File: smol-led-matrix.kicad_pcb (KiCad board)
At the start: 4 copper layers, 46.4 x 20.4 mm, 320 parts, among them J1 USB_C_Receptacle_USB2.0, J2 TagConnect_TC2030_SWD, Q1 FS8205, Q2 AO3401A, SW1 SW_Push, SW2 SW_Push, U1 STM32L433CBTx, U2 TP4054, U3 DW01+G, U4 XC6206P332MR

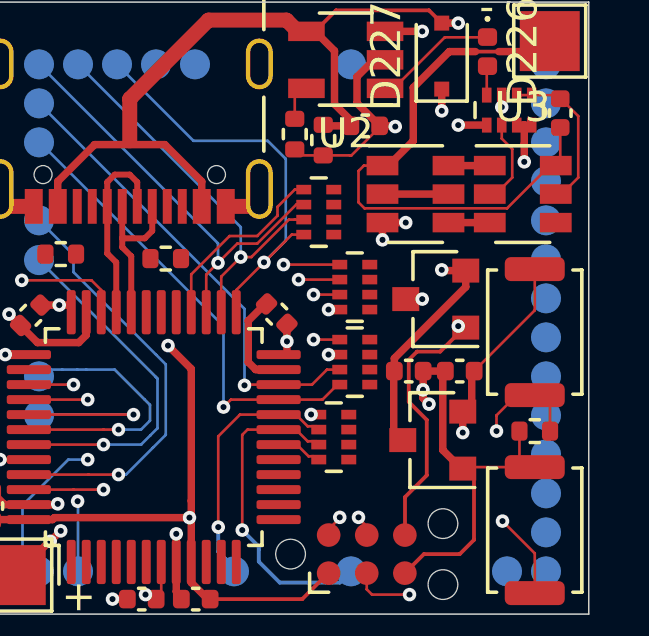
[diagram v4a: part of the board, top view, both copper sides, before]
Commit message: Layout straight forward anode controls
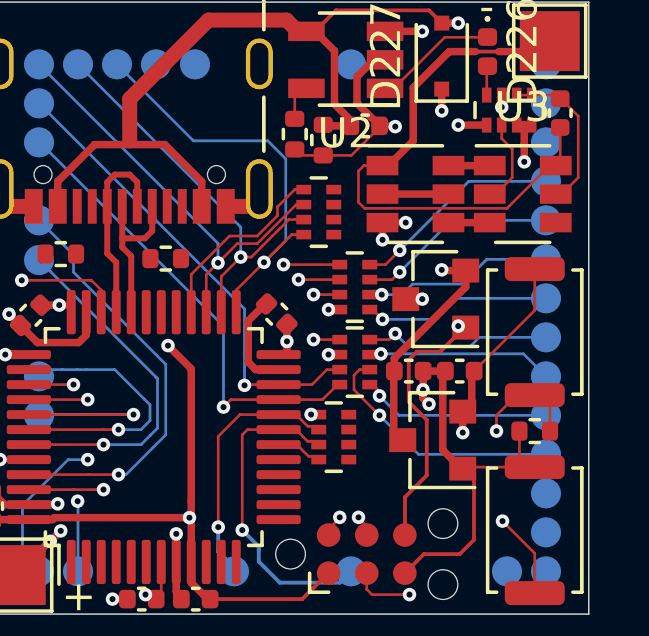
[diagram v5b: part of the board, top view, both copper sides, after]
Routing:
- net /A11: track 19.9 -> 28.3 mm, vias 1 -> 2
- net /A4: track 19.9 -> 26.9 mm, vias 1 -> 2
- net /A5: track 19.9 -> 26.6 mm, vias 1 -> 2
- net /A8: track 19.9 -> 26.6 mm, vias 1 -> 2
- net /A10: track 19.9 -> 26.3 mm, vias 1 -> 2
- net /A6: track 19.9 -> 26.3 mm, vias 1 -> 2
- net /A7: track 19.9 -> 26.2 mm, vias 1 -> 2
- net /A9: track 19.9 -> 26.1 mm, vias 1 -> 2
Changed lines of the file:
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@@
     (thickness 1.6)
     (drawings 11)
-    (tracks 1141)
+    (tracks 1190)
     (zones 0)
     (modules 320)
@@
   (via (at 102.3 103.55) (size 0.45) (drill 0.2) (layers F.Cu B.Cu) (net 6))
   (segment (start 101 103.549999) (end 102.3 103.55) (width 0.09) (layer B.Cu) (net 6))
+  (via (at 139.675 105.85) (size 0.45) (drill 0.2) (layers F.Cu B.Cu) (net 6))
+  (segment (start 139.2 106.325) (end 139.675 105.85) (width 0.09) (layer F.Cu) (net 6))
+  (segment (start 138.675 106.325) (end 139.2 106.325) (width 0.09) (layer F.Cu) (net 6))
+  (segment (start 141.975 103.55) (end 139.675 105.85) (width 0.09) (layer B.Cu) (net 6))
+  (segment (start 144.55 103.55) (end 141.975 103.55) (width 0.09) (layer B.Cu) (net 6))
   (segment (start 106.217947 104.832052) (end 106.867947 104.832053) (width 0.09) (layer F.Cu) (net 7))
   (segment (start 108.132053 104.832053) (end 108.817947 104.832053) (width 0.09) (layer F.Cu) (net 7))
@@
   (via (at 102.3 104.85) (size 0.45) (drill 0.2) (layers F.Cu B.Cu) (net 7))
   (segment (start 101 104.85) (end 102.3 104.85) (width 0.09) (layer B.Cu) (net 7))
+  (via (at 139.675 106.575) (size 0.45) (drill 0.2) (layers F.Cu B.Cu) (net 7))
+  (segment (start 139.425 106.825) (end 139.675 106.575) (width 0.09) (layer F.Cu) (net 7))
+  (segment (start 138.675 106.825) (end 139.425 106.825) (width 0.09) (layer F.Cu) (net 7))
+  (segment (start 141.4 104.85) (end 139.675 106.575) (width 0.09) (layer B.Cu) (net 7))
+  (segment (start 144.55 104.85) (end 141.4 104.85) (width 0.09) (layer B.Cu) (net 7))
   (segment (start 107.517947 106.132053) (end 108.167947 106.132054) (width 0.09) (layer F.Cu) (net 8))
   (segment (start 109.432053 106.132053) (end 110.117946 106.132054) (width 0.09) (layer F.Cu) (net 8))
@@
   (via (at 102.3 106.150001) (size 0.45) (drill 0.2) (layers F.Cu B.Cu) (net 8))
   (segment (start 101 106.15) (end 102.3 106.150001) (width 0.09) (layer B.Cu) (net 8))
+  (via (at 139.075 107.325) (size 0.45) (drill 0.2) (layers F.Cu B.Cu) (net 8))
+  (segment (start 138.675 107.325) (end 139.075 107.325) (width 0.09) (layer F.Cu) (net 8))
+  (segment (start 139.075 107.325) (end 139.75 107.325) (width 0.09) (layer B.Cu) (net 8))
+  (segment (start 139.75 107.325) (end 140.1 106.975) (width 0.09) (layer B.Cu) (net 8))
+  (segment (start 142.575 106.15) (end 141.75 106.975) (width 0.09) (layer B.Cu) (net 8))
+  (segment (start 144.55 106.15) (end 142.575 106.15) (width 0.09) (layer B.Cu) (net 8))
+  (segment (start 140.1 106.975) (end 141.75 106.975) (width 0.09) (layer B.Cu) (net 8))
   (segment (start 108.817948 107.432053) (end 109.467947 107.432053) (width 0.09) (layer F.Cu) (net 9))
   (segment (start 110.732053 107.432053) (end 111.417945 107.432053) (width 0.09) (layer F.Cu) (net 9))
@@
   (via (at 102.3 107.449999) (size 0.45) (drill 0.2) (layers F.Cu B.Cu) (net 9))
   (segment (start 101 107.45) (end 102.3 107.449999) (width 0.09) (layer B.Cu) (net 9))
+  (via (at 139.1 108.15) (size 0.45) (drill 0.2) (layers F.Cu B.Cu) (net 9))
+  (segment (start 138.775 107.825) (end 139.1 108.15) (width 0.09) (layer F.Cu) (net 9))
+  (segment (start 138.675 107.825) (end 138.775 107.825) (width 0.09) (layer F.Cu) (net 9))
+  (segment (start 144.55 107.45) (end 141.425 107.45) (width 0.09) (layer B.Cu) (net 9))
+  (segment (start 140.725 108.15) (end 139.1 108.15) (width 0.09) (layer B.Cu) (net 9))
+  (segment (start 141.425 107.45) (end 140.725 108.15) (width 0.09) (layer B.Cu) (net 9))
   (segment (start 110.117947 108.732053) (end 110.767947 108.732053) (width 0.09) (layer F.Cu) (net 10))
   (segment (start 112.032053 108.732053) (end 112.717947 108.732053) (width 0.09) (layer F.Cu) (net 10))
@@
   (via (at 102.3 108.75) (size 0.45) (drill 0.2) (layers F.Cu B.Cu) (net 10))
   (segment (start 101 108.75) (end 102.3 108.75) (width 0.09) (layer B.Cu) (net 10))
+  (via (at 139.525 108.625) (size 0.45) (drill 0.2) (layers F.Cu B.Cu) (net 10))
+  (segment (start 139.325 108.825) (end 139.525 108.625) (width 0.09) (layer F.Cu) (net 10))
+  (segment (start 138.675 108.825) (end 139.325 108.825) (width 0.09) (layer F.Cu) (net 10))
+  (segment (start 139.525 108.625) (end 139.95 109.05) (width 0.09) (layer B.Cu) (net 10))
+  (segment (start 144.25 109.05) (end 144.55 108.75) (width 0.09) (layer B.Cu) (net 10))
+  (segment (start 144.55 108.75) (end 142.325 108.75) (width 0.09) (layer B.Cu) (net 10))
+  (segment (start 142.325 108.75) (end 142.025 109.05) (width 0.09) (layer B.Cu) (net 10))
+  (segment (start 139.95 109.05) (end 142.025 109.05) (width 0.09) (layer B.Cu) (net 10))
   (segment (start 111.417947 110.032053) (end 112.067947 110.032053) (width 0.09) (layer F.Cu) (net 11))
   (segment (start 113.332053 110.032053) (end 114.017947 110.032054) (width 0.09) (layer F.Cu) (net 11))
@@
   (via (at 102.3 110.05) (size 0.45) (drill 0.2) (layers F.Cu B.Cu) (net 11))
   (segment (start 100.999999 110.050001) (end 102.3 110.05) (width 0.09) (layer B.Cu) (net 11))
+  (via (at 139.05 109.3) (size 0.45) (drill 0.2) (layers F.Cu B.Cu) (net 11))
+  (segment (start 139.025 109.325) (end 139.05 109.3) (width 0.09) (layer F.Cu) (net 11))
+  (segment (start 138.675 109.325) (end 139.025 109.325) (width 0.09) (layer F.Cu) (net 11))
+  (segment (start 139.05 109.3) (end 143.8 109.3) (width 0.09) (layer B.Cu) (net 11))
+  (segment (start 143.8 109.3) (end 144.55 110.05) (width 0.09) (layer B.Cu) (net 11))
   (segment (start 112.717947 111.332052) (end 113.367947 111.332053) (width 0.09) (layer F.Cu) (net 12))
   (segment (start 114.632053 111.332053) (end 115.317945 111.332053) (width 0.09) (layer F.Cu) (net 12))
@@
   (via (at 102.3 111.35) (size 0.45) (drill 0.2) (layers F.Cu B.Cu) (net 12))
   (segment (start 101 111.35) (end 102.3 111.35) (width 0.09) (layer B.Cu) (net 12))
+  (segment (start 138.675 110.325) (end 138.775 110.325) (width 0.09) (layer F.Cu) (net 12))
+  (via (at 139 110.7) (size 0.45) (drill 0.2) (layers F.Cu B.Cu) (net 12))
+  (segment (start 139 110.55) (end 139 110.7) (width 0.09) (layer F.Cu) (net 12))
+  (segment (start 138.775 110.325) (end 139 110.55) (width 0.09) (layer F.Cu) (net 12))
+  (segment (start 139.65 111.35) (end 139 110.7) (width 0.09) (layer B.Cu) (net 12))
+  (segment (start 144.55 111.35) (end 139.65 111.35) (width 0.09) (layer B.Cu) (net 12))
   (segment (start 114.017947 112.632053) (end 114.667947 112.632053) (width 0.09) (layer F.Cu) (net 13))
   (segment (start 115.932053 112.632053) (end 116.617947 112.632053) (width 0.09) (layer F.Cu) (net 13))
@@
   (via (at 102.3 112.65) (size 0.45) (drill 0.2) (layers F.Cu B.Cu) (net 13))
   (segment (start 101 112.65) (end 102.3 112.65) (width 0.09) (layer B.Cu) (net 13))
+  (segment (start 138.335 109.825) (end 138.15 110.01) (width 0.09) (layer F.Cu) (net 13))
+  (segment (start 138.675 109.825) (end 138.335 109.825) (width 0.09) (layer F.Cu) (net 13))
+  (via (at 139 111.35) (size 0.45) (drill 0.2) (layers F.Cu B.Cu) (net 13))
+  (segment (start 140.3 112.65) (end 139 111.35) (width 0.09) (layer B.Cu) (net 13))
+  (segment (start 144.55 112.65) (end 140.3 112.65) (width 0.09) (layer B.Cu) (net 13))
+  (segment (start 138.15 110.5) (end 138.15 110.01) (width 0.09) (layer F.Cu) (net 13))
+  (segment (start 139 111.35) (end 138.15 110.5) (width 0.09) (layer F.Cu) (net 13))
   (segment (start 115.317948 113.932053) (end 115.967947 113.932053) (width 0.09) (layer F.Cu) (net 14))
   (segment (start 117.232053 113.932053) (end 117.917947 113.932054) (width 0.09) (layer F.Cu) (net 14))

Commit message: Finish control board layout
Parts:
- moved R4 0.38 mm to (128.0, 105.9)
- moved R3 0.34 mm to (132.2, 105.9)
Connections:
- net Net-(R5-Pad2) renamed /BOOT0
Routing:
- net /A0: track 19.1 -> 46.6 mm, vias 1 -> 2
- net /A1: track 21.8 -> 41.3 mm, vias 1 -> 2
- net /A2: track 19.9 -> 38.0 mm, vias 1 -> 2
- net /A14: track 18.2 -> 35.7 mm, vias 1 -> 3
- net /A13: track 19.9 -> 36.6 mm, vias 1 -> 3
- net /A3: track 19.9 -> 35.2 mm, vias 1 -> 2
- net /K9: track 33.6 -> 48.4 mm
- net /K0: track 21.1 -> 34.4 mm, vias 15 -> 16
- net /A12: track 19.9 -> 32.6 mm, vias 1 -> 3
- net /A15: track 40.0 -> 47.3 mm, vias 15 -> 16
- net GND: track 38.0 -> 45.2 mm, vias 10 -> 11
- net Net-(J1-PadB5): track 0.00 -> 1.72 mm
- net Net-(J1-PadA5): track 0.00 -> 1.63 mm

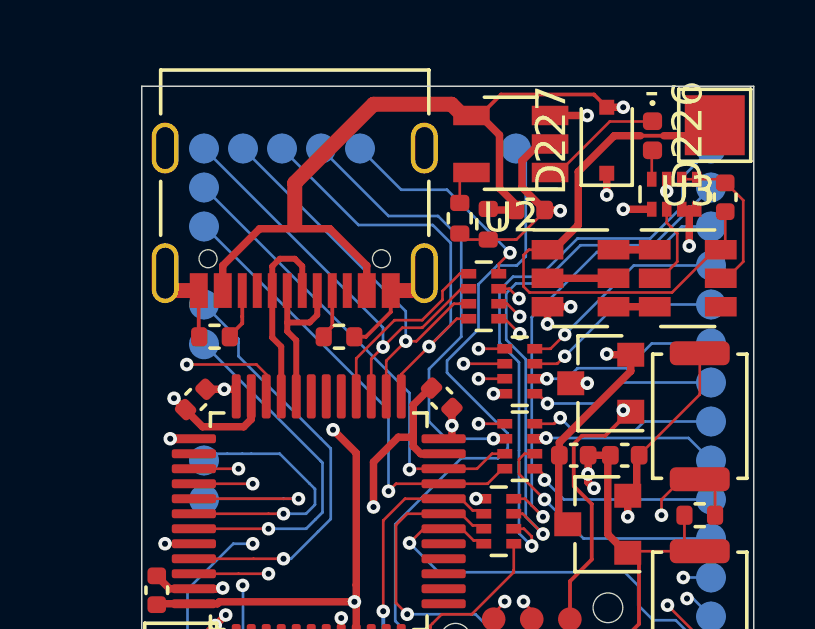
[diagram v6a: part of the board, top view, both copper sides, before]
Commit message: Maximize clearance between USB C pull-downs and connector
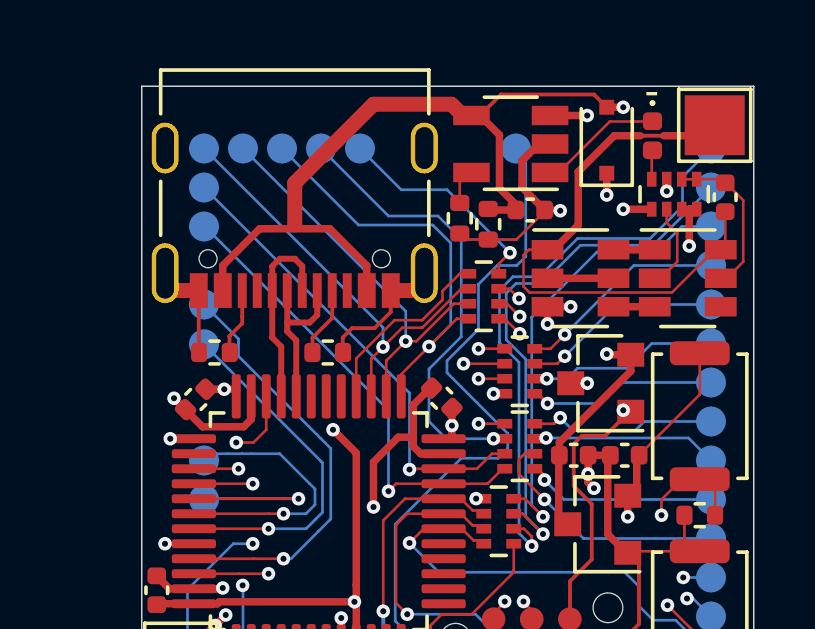
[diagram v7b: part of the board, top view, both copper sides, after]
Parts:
- moved R3 0.65 mm to (131.8, 106.5)
- moved R4 0.53 mm to (128.0, 106.5)
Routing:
- net Net-(J2-Pad2): track 24.5 -> 21.4 mm
- net GND: track 45.2 -> 46.6 mm
- net Net-(J1-PadA5): track 1.63 -> 2.34 mm
- net Net-(J1-PadB5): track 1.72 -> 2.27 mm

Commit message: Cleanup layout
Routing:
- net /K9: track 48.4 -> 46.9 mm
- net /A0: track 46.6 -> 45.1 mm
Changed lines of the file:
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@@
     (thickness 1.6)
     (drawings 11)
-    (tracks 1347)
+    (tracks 1348)
     (zones 0)
     (modules 320)
@@
   )
   (setup
-    (last_trace_width 0.127)
+    (last_trace_width 0.25)
     (user_trace_width 0.127)
     (user_trace_width 0.2)
@@
   (segment (start 135.6375 112.325) (end 134.975 112.325) (width 0.09) (layer F.Cu) (net 2))
   (segment (start 144.55 116.55) (end 143.375 115.375) (width 0.09) (layer B.Cu) (net 2))
-  (segment (start 143.375 115.375) (end 142.625 115.375) (width 0.09) (layer B.Cu) (net 2))
-  (segment (start 142.625 115.375) (end 142.125 114.875) (width 0.09) (layer B.Cu) (net 2))
-  (segment (start 142.125 114.875) (end 142.125 114.225) (width 0.09) (layer B.Cu) (net 2))
-  (segment (start 142.125 114.225) (end 141.675 113.775) (width 0.09) (layer B.Cu) (net 2))
   (segment (start 135.475 113.775) (end 134.5 112.8) (width 0.09) (layer B.Cu) (net 2))
-  (segment (start 141.675 113.775) (end 135.475 113.775) (width 0.09) (layer B.Cu) (net 2))
+  (segment (start 140.6 113.775) (end 141.225 113.775) (width 0.09) (layer B.Cu) (net 2))
+  (segment (start 140.6 113.775) (end 135.475 113.775) (width 0.09) (layer B.Cu) (net 2))
+  (segment (start 142.05 114.6) (end 142.825 115.375) (width 0.09) (layer B.Cu) (net 2))
+  (segment (start 143.375 115.375) (end 142.825 115.375) (width 0.09) (layer B.Cu) (net 2))
+  (segment (start 141.225 113.775) (end 142.05 114.6) (width 0.09) (layer B.Cu) (net 2))
+  (segment (start 142.05 114.6) (end 142.125 114.675) (width 0.09) (layer B.Cu) (net 2))
   (segment (start 102.932053 99.632053) (end 103.617947 99.632054) (width 0.09) (layer F.Cu) (net 3))
   (segment (start 102.415 99.115) (end 102.932053 99.632053) (width 0.09) (layer F.Cu) (net 3))
@@
   (segment (start 134.025 112.175) (end 136.225 109.975) (width 0.09) (layer B.Cu) (net 17))
   (segment (start 136.225 109.975) (end 137.45 109.975) (width 0.09) (layer B.Cu) (net 17))
-  (segment (start 137.775 109.65) (end 137.775 109.15) (width 0.09) (layer B.Cu) (net 17))
-  (segment (start 137.45 109.975) (end 137.775 109.65) (width 0.09) (layer B.Cu) (net 17))
-  (segment (start 137.775 109.15) (end 135.75 107.125) (width 0.09) (layer B.Cu) (net 17))
-  (segment (start 135.75 107.125) (end 135.75 106.725) (width 0.09) (layer B.Cu) (net 17))
-  (segment (start 135.75 106.725) (end 136.8 105.675) (width 0.09) (layer B.Cu) (net 17))
-  (segment (start 136.8 105.675) (end 136.8 104.175) (width 0.09) (layer B.Cu) (net 17))
-  (segment (start 136.8 104.175) (end 137.425 103.55) (width 0.09) (layer B.Cu) (net 17))
-  (segment (start 137.425 103.55) (end 138.075 103.55) (width 0.09) (layer B.Cu) (net 17))
-  (segment (start 138.075 103.55) (end 138.375 103.25) (width 0.09) (layer B.Cu) (net 17))
-  (segment (start 138.375 103.25) (end 138.375 100) (width 0.09) (layer B.Cu) (net 17))
   (segment (start 138.375 100) (end 138.05 99.675) (width 0.09) (layer B.Cu) (net 17))
+  (segment (start 138.375 103.2) (end 138.375 103) (width 0.09) (layer B.Cu) (net 17))
+  (segment (start 137.95 106.85) (end 137.3 106.2) (width 0.09) (layer B.Cu) (net 17))
+  (segment (start 137.95 109.5) (end 137.95 106.85) (width 0.09) (layer B.Cu) (net 17))
+  (segment (start 137.475 109.975) (end 137.95 109.5) (width 0.09) (layer B.Cu) (net 17))
+  (segment (start 137.3 106.2) (end 137.3 104.275) (width 0.09) (layer B.Cu) (net 17))
+  (segment (start 137.45 109.975) (end 137.475 109.975) (width 0.09) (layer B.Cu) (net 17))
+  (segment (start 138.375 103) (end 138.375 100) (width 0.09) (layer B.Cu) (net 17))
+  (segment (start 137.3 104.275) (end 138.375 103.2) (width 0.09) (layer B.Cu) (net 17))
   (via (at 101.635 99.025) (size 0.45) (drill 0.2) (layers F.Cu B.Cu) (net 18))
   (segment (start 101.635 99.025) (end 101.635 100.325001) (width 0.127) (layer In2.Cu) (net 18))
@@
   (segment (start 136.8 109.325) (end 137.3 109.325) (width 0.127) (layer In2.Cu) (net 26))
   (segment (start 132.303501 113.821499) (end 136.8 109.325) (width 0.127) (layer In2.Cu) (net 26))
-  (segment (start 137.3 109.325) (end 135.725 109.325) (width 0.09) (layer B.Cu) (net 26))
-  (segment (start 135.725 109.325) (end 135.15 108.75) (width 0.09) (layer B.Cu) (net 26))
-  (segment (start 135.15 108.75) (end 135.15 107) (width 0.09) (layer B.Cu) (net 26))
-  (segment (start 135.15 107) (end 136.225 105.925) (width 0.09) (layer B.Cu) (net 26))
   (segment (start 136.225 105.925) (end 136.225 102.675) (width 0.09) (layer B.Cu) (net 26))
   (segment (start 136.225 102.675) (end 135.45 101.9) (width 0.09) (layer B.Cu) (net 26))
   (segment (start 135.45 101.9) (end 133.8 101.9) (width 0.09) (layer B.Cu) (net 26))
   (segment (start 133.8 101.9) (end 131.55 99.65) (width 0.09) (layer B.Cu) (net 26))
+  (segment (start 137.3 109.325) (end 137.3 108.525) (width 0.09) (layer B.Cu) (net 26))
+  (segment (start 135.9 107.125) (end 135.9 106.25) (width 0.09) (layer B.Cu) (net 26))
+  (segment (start 137.3 108.525) (end 135.9 107.125) (width 0.09) (layer B.Cu) (net 26))
+  (segment (start 135.9 106.25) (end 136.225 105.925) (width 0.09) (layer B.Cu) (net 26))
   (via (at 113.335 99.025) (size 0.45) (drill 0.2) (layers F.Cu B.Cu) (net 27))
   (segment (start 113.335 99.025) (end 113.335 100.325) (width 0.127) (layer In2.Cu) (net 27))
@@
   (segment (start 141.825 108.975) (end 141.05 108.975) (width 0.25) (layer In1.Cu) (net 66))
   (segment (start 128.025 115.55) (end 128.375 115.2) (width 0.25) (layer F.Cu) (net 66))
-  (segment (start 141.825 108.975) (end 141.825 110.7) (width 0.25) (layer In1.Cu) (net 66))
-  (segment (start 141.825 110.7) (end 139.175 113.35) (width 0.25) (layer In1.Cu) (net 66))
   (via (at 143.825 102.9) (size 0.45) (drill 0.2) (layers F.Cu B.Cu) (net 66))
   (segment (start 143.825 102.3) (end 143.825 102.9) (width 0.25) (layer F.Cu) (net 66))
   (segment (start 143.825 102.9) (end 143.825 107.75) (width 0.25) (layer In1.Cu) (net 66))
   (segment (start 128.375 115.2) (end 130.425 115.2) (width 0.25) (layer In1.Cu) (net 66))
-  (segment (start 130.425 115.2) (end 132.275 113.35) (width 0.25) (layer In1.Cu) (net 66))
-  (segment (start 139.175 113.35) (end 132.275 113.35) (width 0.25) (layer In1.Cu) (net 66))
+  (segment (start 131.9625 113.6625) (end 132.125 113.5) (width 0.25) (layer In1.Cu) (net 66))
+  (segment (start 130.425 115.2) (end 131.9625 113.6625) (width 0.25) (layer In1.Cu) (net 66))
+  (segment (start 141.825 110.7) (end 141.825 108.975) (width 0.25) (layer In1.Cu) (net 66))
+  (segment (start 139.075 113.45) (end 141.825 110.7) (width 0.25) (layer In1.Cu) (net 66))
+  (segment (start 132.175 113.45) (end 139.075 113.45) (width 0.25) (layer In1.Cu) (net 66))
+  (segment (start 131.9625 113.6625) (end 132.175 113.45) (width 0.25) (layer In1.Cu) (net 66))
   (segment (start 139.775 112.175) (end 139.475 111.875) (width 0.25) (layer F.Cu) (net 67))
   (segment (start 139.475 111.875) (end 139.475 109.875) (width 0.25) (layer F.Cu) (net 67))
